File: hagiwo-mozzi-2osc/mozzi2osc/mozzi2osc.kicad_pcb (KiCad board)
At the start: 2 copper layers, 40.2 x 109.2 mm, 35 parts, among them J1 AudioJack2, J2 AudioJack2, J3 AudioJack2, J4 Conn_02x05_Odd_Even, SW1 SW_SPDT_MSM, U1 TL072

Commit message: i dont know what im doing
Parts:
- added J1: AudioJack2, Connector_Audio:Jack_3.5mm_QingPu_WQP-PJ398SM_Vertical_CircularHoles, F.Cu at (81.3, 109.9)
- added J2: AudioJack2, Connector_Audio:Jack_3.5mm_QingPu_WQP-PJ398SM_Vertical_CircularHoles, F.Cu at (81.3, 127.0)
- added J3: AudioJack2, Connector_Audio:Jack_3.5mm_QingPu_WQP-PJ398SM_Vertical_CircularHoles, F.Cu at (81.3, 144.8)
- added RV1: 100k, Potentiometer_THT:Potentiometer_Alpha_RD901F-40-00D_Single_Vertical, F.Cu at (78.8, 54.0)
- added RV2: 100k, Potentiometer_THT:Potentiometer_Alpha_RD901F-40-00D_Single_Vertical, F.Cu at (78.8, 69.2)
- added RV3: 100k, Potentiometer_THT:Potentiometer_Alpha_RD901F-40-00D_Single_Vertical, F.Cu at (78.8, 84.5)
- added SW1: SW_SPDT_MSM, rpaz:SW_NKK_D22012P, F.Cu at (81.3, 91.4)
- D2: moved to F.Cu
- moved D2 114.4 mm to (166.4, 101.6), turned to -90 degrees
- moved D4 108.6 mm to (170.2, 125.7)
- moved R7 108.1 mm to (171.4, 106.7)
- moved C6 106.8 mm to (144.8, 83.8)
- moved C7 106.8 mm to (144.8, 88.9)
- moved D1 106.8 mm to (138.4, 124.5)
- moved D6 106.8 mm to (141.3, 119.0)
- moved J1 106.8 mm to (154.9, 104.8)
- moved J2 106.8 mm to (154.9, 121.9)
- moved J3 106.8 mm to (154.9, 139.7)
- moved J4 106.8 mm to (170.2, 83.8)
- moved R10 106.8 mm to (142.2, 68.6)
- moved R11 106.8 mm to (142.2, 129.5)
- moved R4 106.8 mm to (162.6, 116.8)
- moved R6 106.8 mm to (162.6, 96.5)
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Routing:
- net V/Oct: track 67.9 -> 79.4 mm
- net CV: track 88.6 -> 82.0 mm
- net +5V: track 119.0 -> 115.9 mm
- net Net-(J2-PadT): track 6.67 -> 7.94 mm
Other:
- board size 40.2 x 109.2 mm -> 114.1 x 133.3 mm

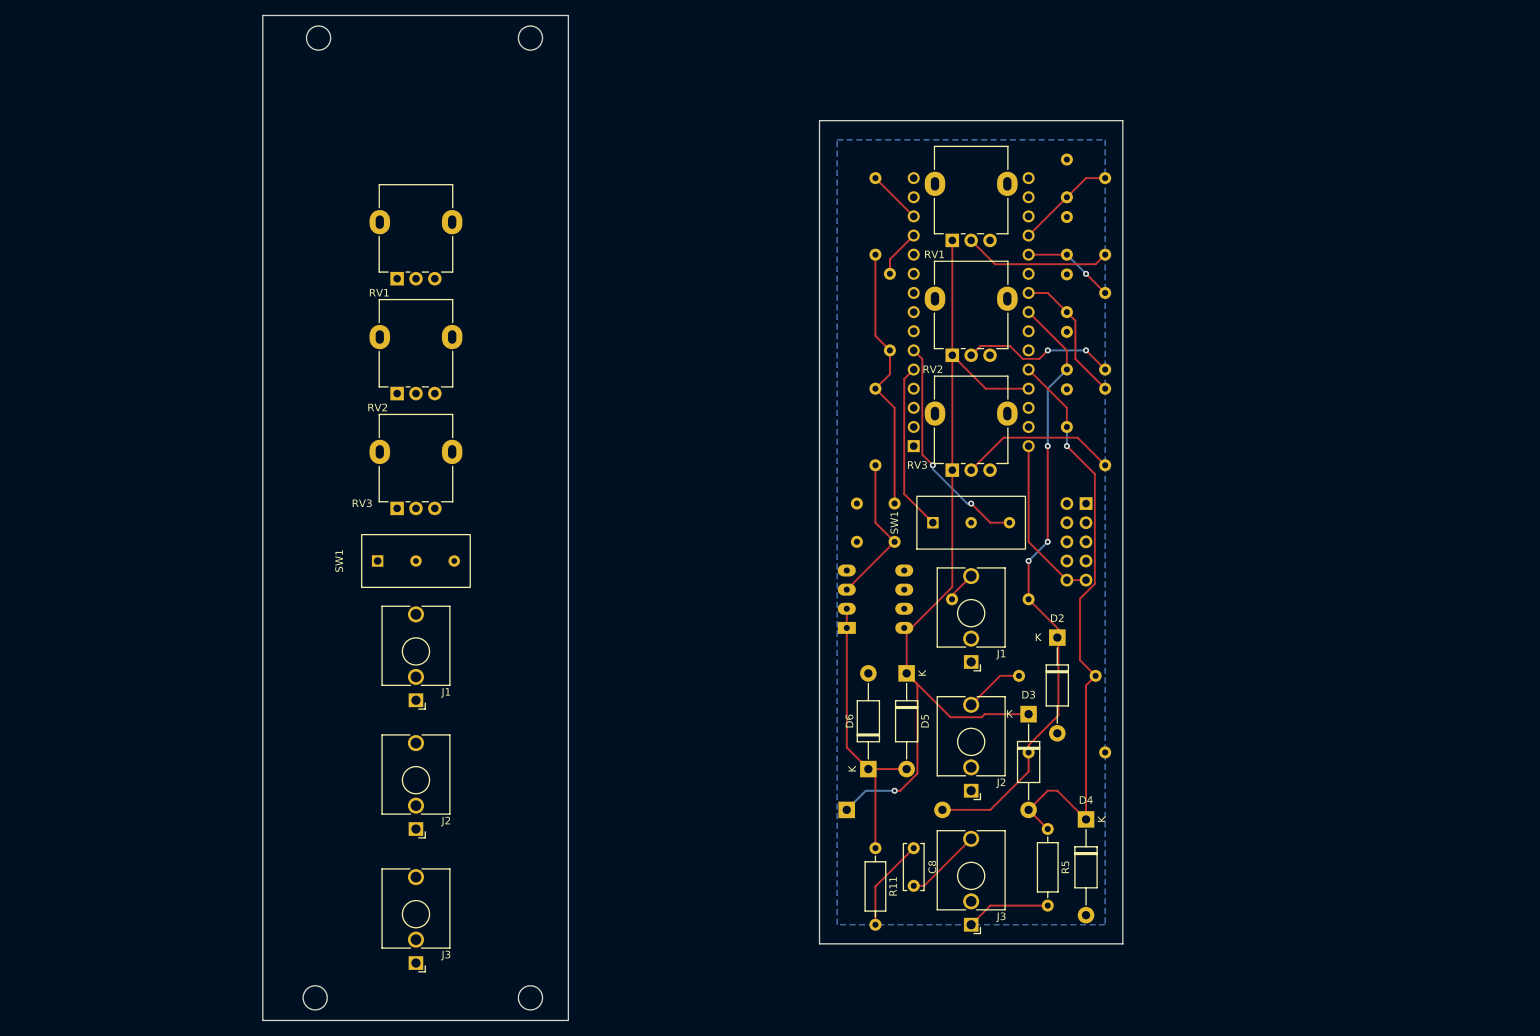
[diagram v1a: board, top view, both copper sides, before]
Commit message: panelize 2osc
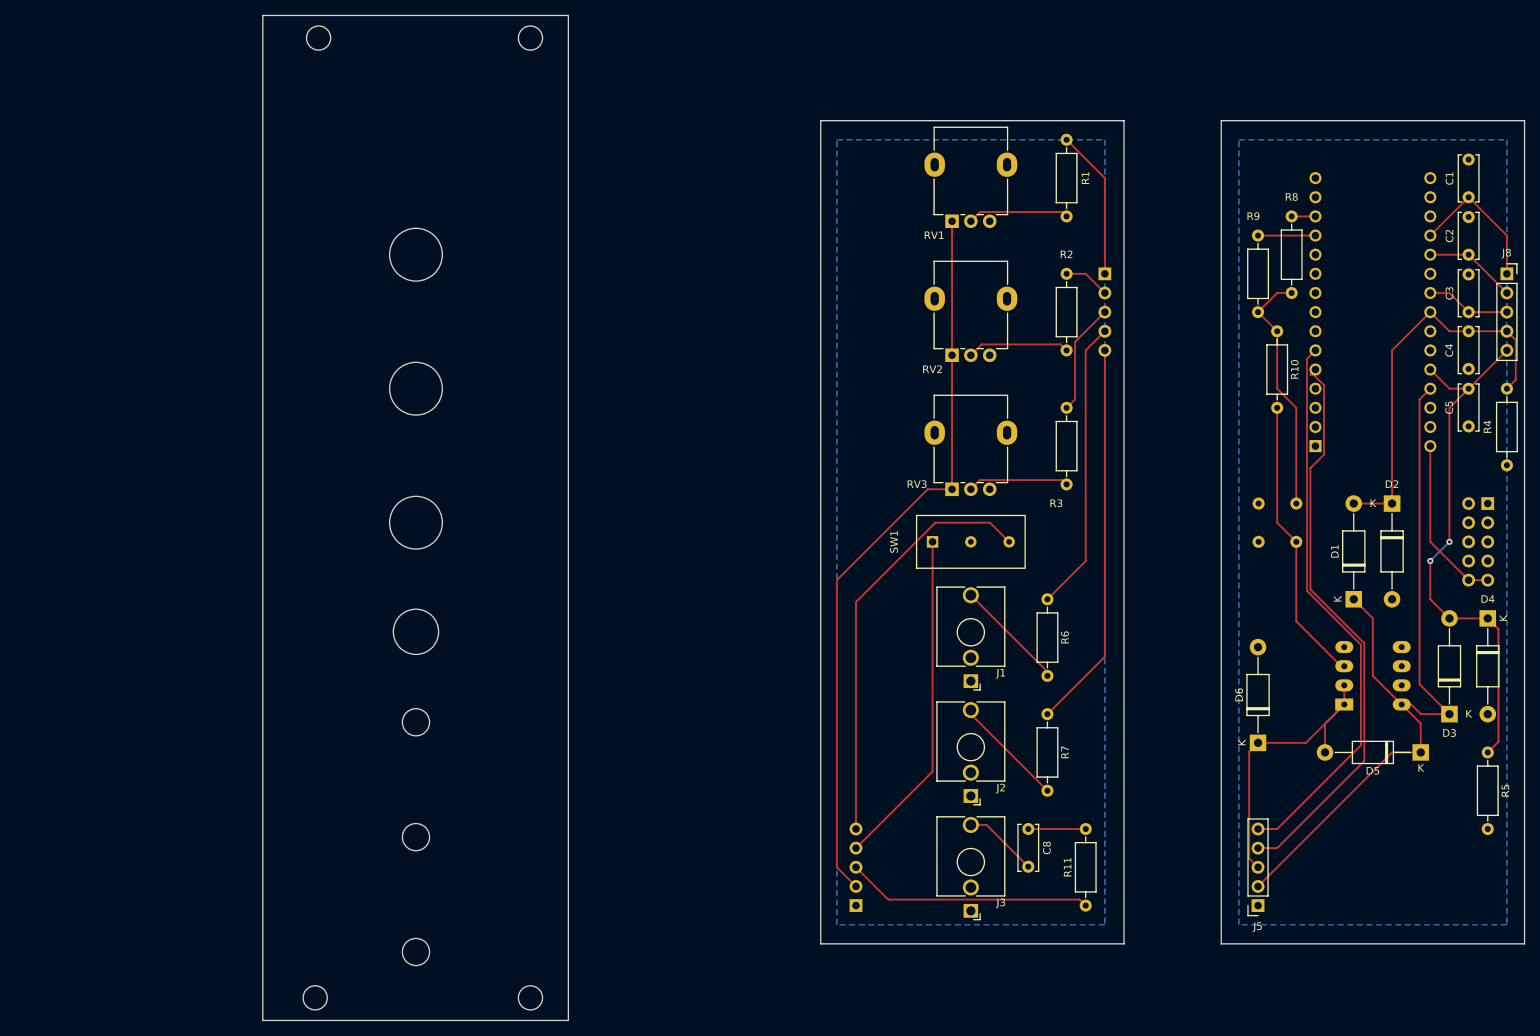
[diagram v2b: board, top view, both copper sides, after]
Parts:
- removed the J1 at (81.3, 109.9)
- removed the J2 at (81.3, 127.0)
- removed the J3 at (81.3, 144.8)
- removed the RV1 at (78.8, 54.0)
- removed the RV2 at (78.8, 69.2)
- removed the RV3 at (78.8, 84.5)
- removed the SW1 at (81.3, 91.4)
- added J5: Conn_01x05_Female, Connector_PinSocket_2.54mm:PinSocket_1x05_P2.54mm_Vertical, F.Cu at (193.0, 137.2)
- added J6: Conn_01x05_Male, Connector_PinHeader_2.54mm:PinHeader_1x05_P2.54mm_Vertical, B.Cu at (139.7, 137.2)
- added J7: Conn_01x05_Male, Connector_PinHeader_2.54mm:PinHeader_1x05_P2.54mm_Vertical, B.Cu at (172.7, 53.3)
- added J8: Conn_01x05_Female, Connector_PinSocket_2.54mm:PinSocket_1x05_P2.54mm_Vertical, F.Cu at (226.0, 53.3)
- C1, C2, C3, C4, C5, D1, R1, R10, R2, R3, R4, R6, R7, R8, R9: moved to F.Cu
- moved R4 79.7 mm to (226.0, 68.6), turned to -90 degrees
- moved D1 72.8 mm to (205.7, 96.5), turned to 90 degrees
- moved D5 69.0 mm to (214.6, 116.8), turned to 180 degrees
- moved U1 66.8 mm to (204.4, 110.5)
- moved D4 59.6 mm to (223.5, 99.1)
- moved R5 59.3 mm to (223.5, 116.8)
- moved D3 55.8 mm to (218.4, 111.8), turned to 90 degrees
- moved R8 55.5 mm to (197.5, 45.7)
- moved R10 53.8 mm to (195.5, 61.0)
- moved C4 53.5 mm to (220.9, 61.0), turned to -90 degrees
- moved C5 53.5 mm to (220.9, 68.6), turned to -90 degrees
- moved A1 53.3 mm to (200.6, 76.2)
- moved C1 53.3 mm to (220.9, 43.2)
- moved C2 53.3 mm to (220.9, 50.8)
- moved C3 53.3 mm to (220.9, 58.4)
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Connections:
- net Net-(D5-Pad2) renamed Out
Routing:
- net OctDown: track 29.9 -> 129.9 mm, vias 2 -> 0
- net OctUp: track 22.4 -> 120.6 mm
- net +5V: track 115.9 -> 202.8 mm, vias 1 -> 0
- net V/Oct: track 79.4 -> 122.4 mm, vias 1 -> 2
- net Out: track 38.4 -> 73.6 mm
- net Osc1Freq: track 13.3 -> 39.3 mm
- net Net-(C7-Pad1): track 20.2 -> 38.2 mm
- net GND: track 11.2 -> 0.00 mm
- net Net-(J1-PadT): track 3.59 -> 14.4 mm
- net CV: track 82.0 -> 91.1 mm, vias 3 -> 0
- net Net-(R3-Pad1): track 21.1 -> 13.4 mm
- net Wave: track 18.4 -> 26.0 mm
- net Net-(R2-Pad1): track 20.5 -> 13.6 mm, vias 2 -> 0
- net Net-(J2-PadT): track 7.94 -> 14.4 mm
- net Net-(R1-Pad1): track 19.6 -> 13.4 mm
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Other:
- board size 114.1 x 133.3 mm -> 167.4 x 133.3 mm
